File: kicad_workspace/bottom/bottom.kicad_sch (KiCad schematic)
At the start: 11 parts, among them M1 N20_MOTOR_EXTENDED_SHAFT, M2 N20_MOTOR_EXTENDED_SHAFT, U1 DRV8833PWP, U2 ULTRASOUND_T_R, U3 ATmega4809-A

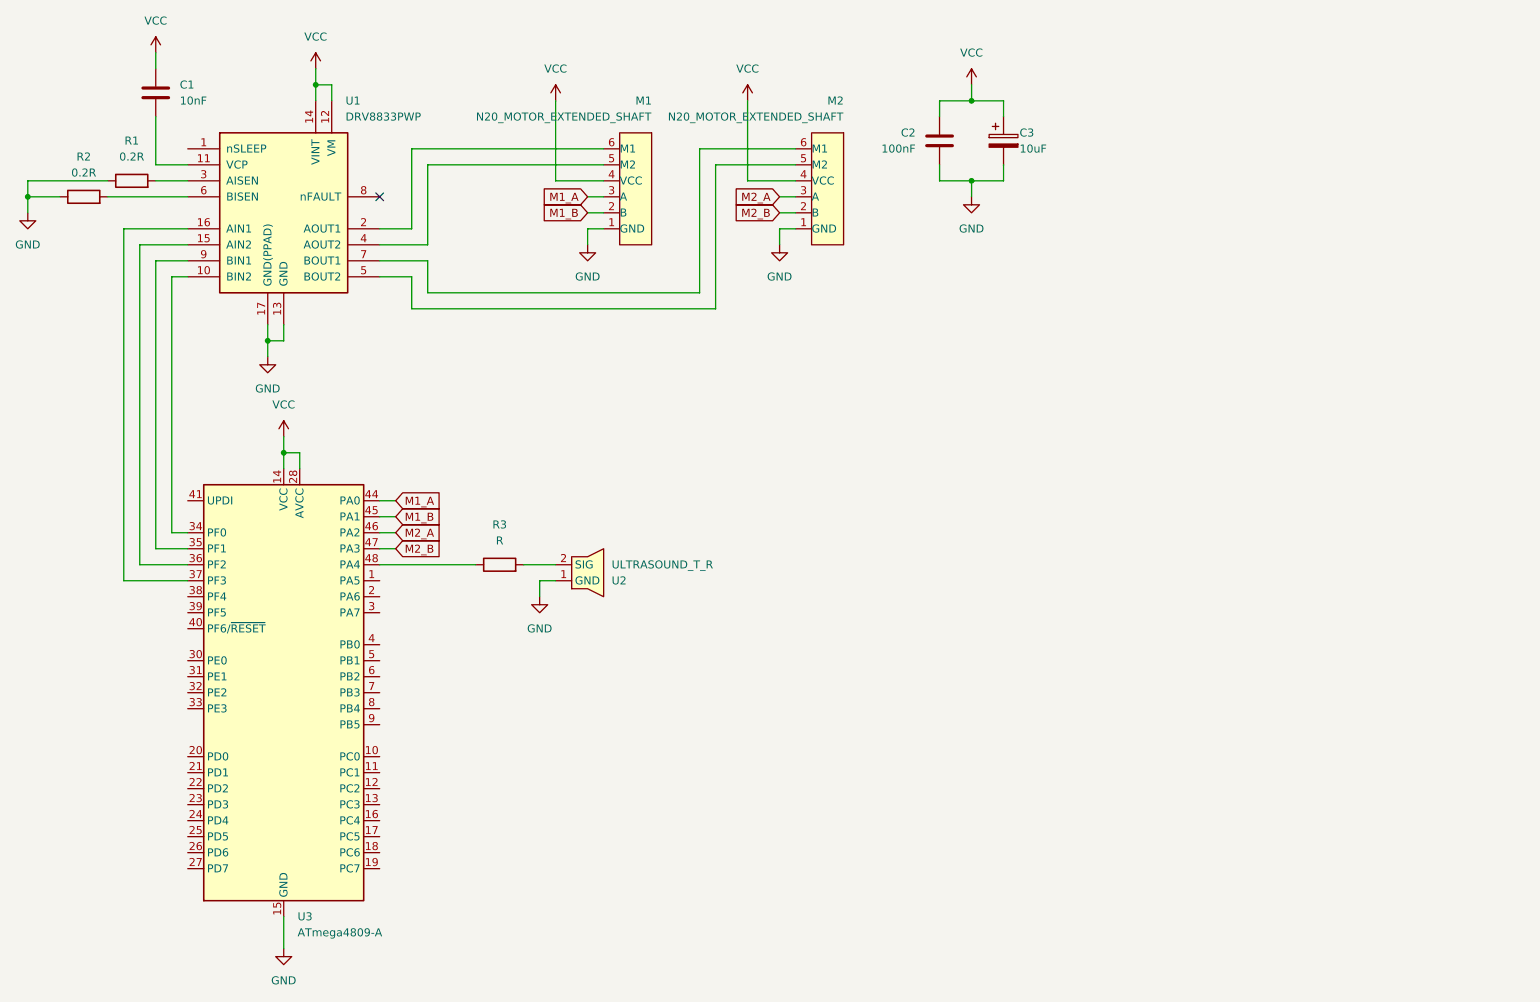
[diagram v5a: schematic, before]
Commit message: add bno055 - acc ic
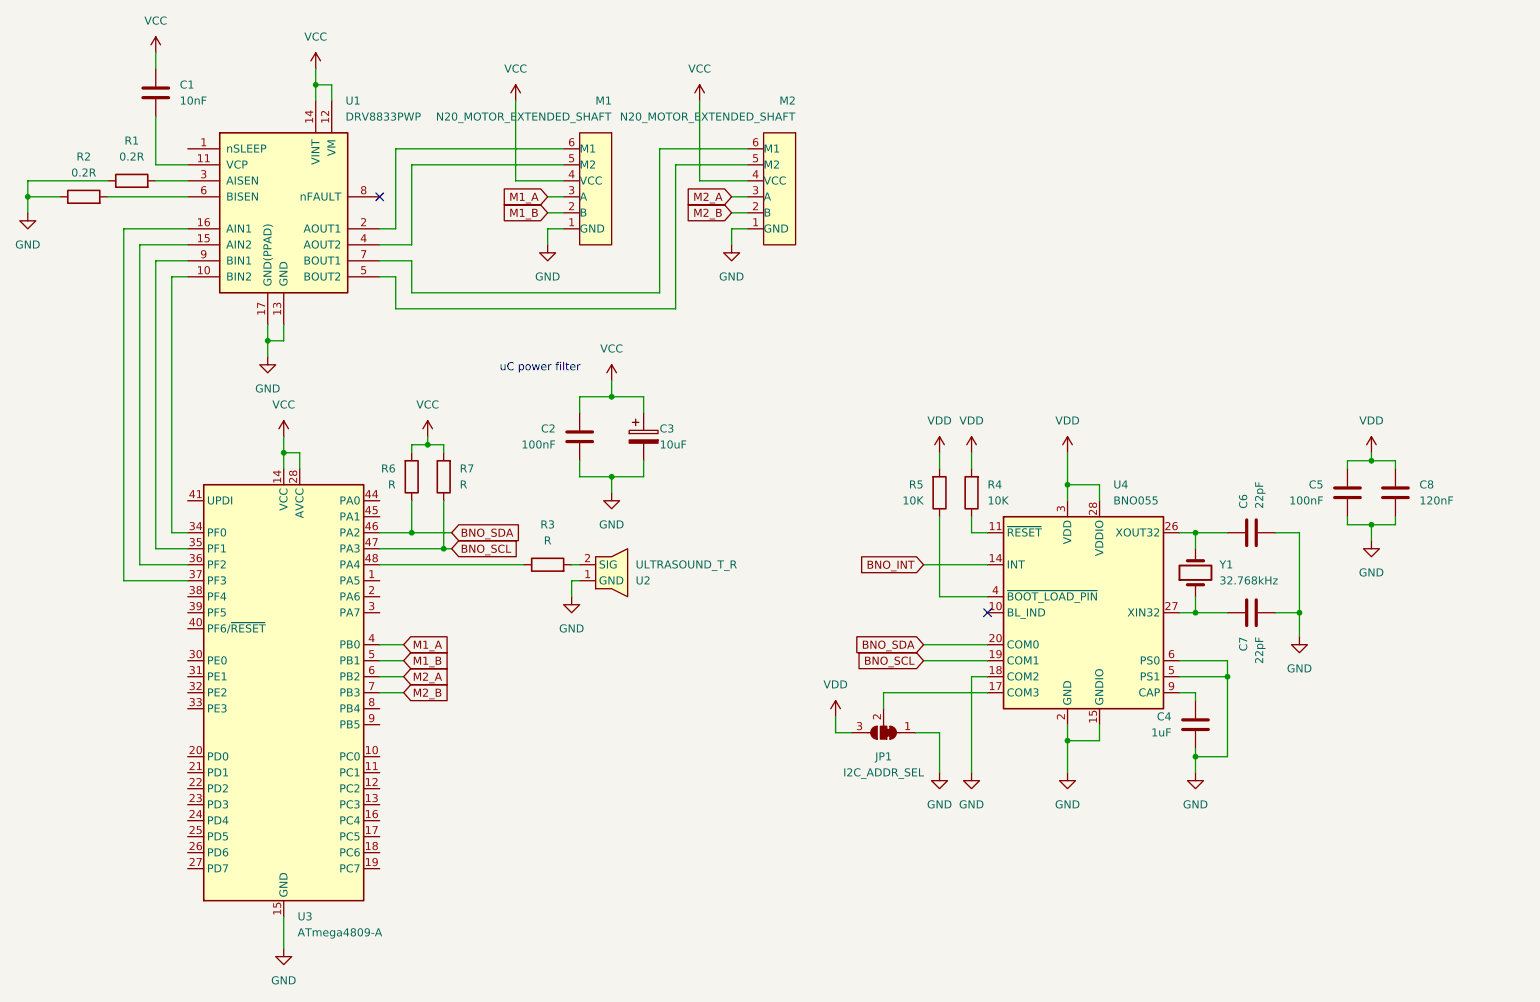
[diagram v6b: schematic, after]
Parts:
- added C4: 1uF, symbol Device:C
- added C5: 100nF, symbol Device:C
- added C6, C7: 22pF, symbol Device:C
- added C8: 120nF, symbol Device:C
- added JP1: I2C_ADDR_SEL, Jumper:SolderJumper-3_P1.3mm_Bridged12_Pad1.0x1.5mm_NumberLabels, symbol Jumper:SolderJumper_3_Bridged12
- added R4, R5: 10K, symbol Device:R
- added R6, R7: R, symbol Device:R
- added U4: BNO055, Package_LGA:LGA-28_5.2x3.8mm_P0.5mm, symbol Sensor_Motion:BNO055
- added Y1: 32.768kHz, Crystal:Crystal_SMD_MicroCrystal_CM9V-T1A-2Pin_1.6x1.0mm, symbol Device:Crystal
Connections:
- net GND: now also C4.2, C5.2, C6.2, C7.2, C8.2, JP1.1 (A), U4.15 (GNDIO), U4.16 (GNDIO), U4.18 (COM2), U4.2 (GND), U4.25 (GNDIO), U4.5 (PS1), U4.6 (PS0)
- net M1_A: now also U3.4 (PB0); no longer U3.44 (PA0)
- net M1_B: now also U3.5 (PB1); no longer U3.45 (PA1)
- net M2_A: now also U3.6 (PB2); no longer U3.46 (PA2)
- net M2_B: now also U3.7 (PB3); no longer U3.47 (PA3)
- net VCC: now also R6.2, R7.2
- new net: C7.1, U4.27 (XIN32), Y1.1
- new net: R4.1, U4.11 (~{RESET})
- new net: C4.1, U4.9 (CAP)
- new net: C6.1, U4.26 (XOUT32), Y1.2
- new net: R5.1, U4.4 (~{BOOT_LOAD_PIN})
- new net: JP1.2 (C), U4.17 (COM3)
- new net BNO_INT: U4.14 (INT)
- new net BNO_SCL: R7.1, U3.47 (PA3), U4.19 (COM1)
- new net BNO_SDA: R6.1, U3.46 (PA2), U4.20 (COM0)
- new net VDD: C5.1, C8.1, JP1.3 (B), R4.2, R5.2, U4.28 (VDDIO), U4.3 (VDD)
- no-connect marks 1 -> 2
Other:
- note added: "uC power filter"
- moved on the sheet: C2, C3, M1, M2, R3, U2

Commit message: small schematic fixes (NC)
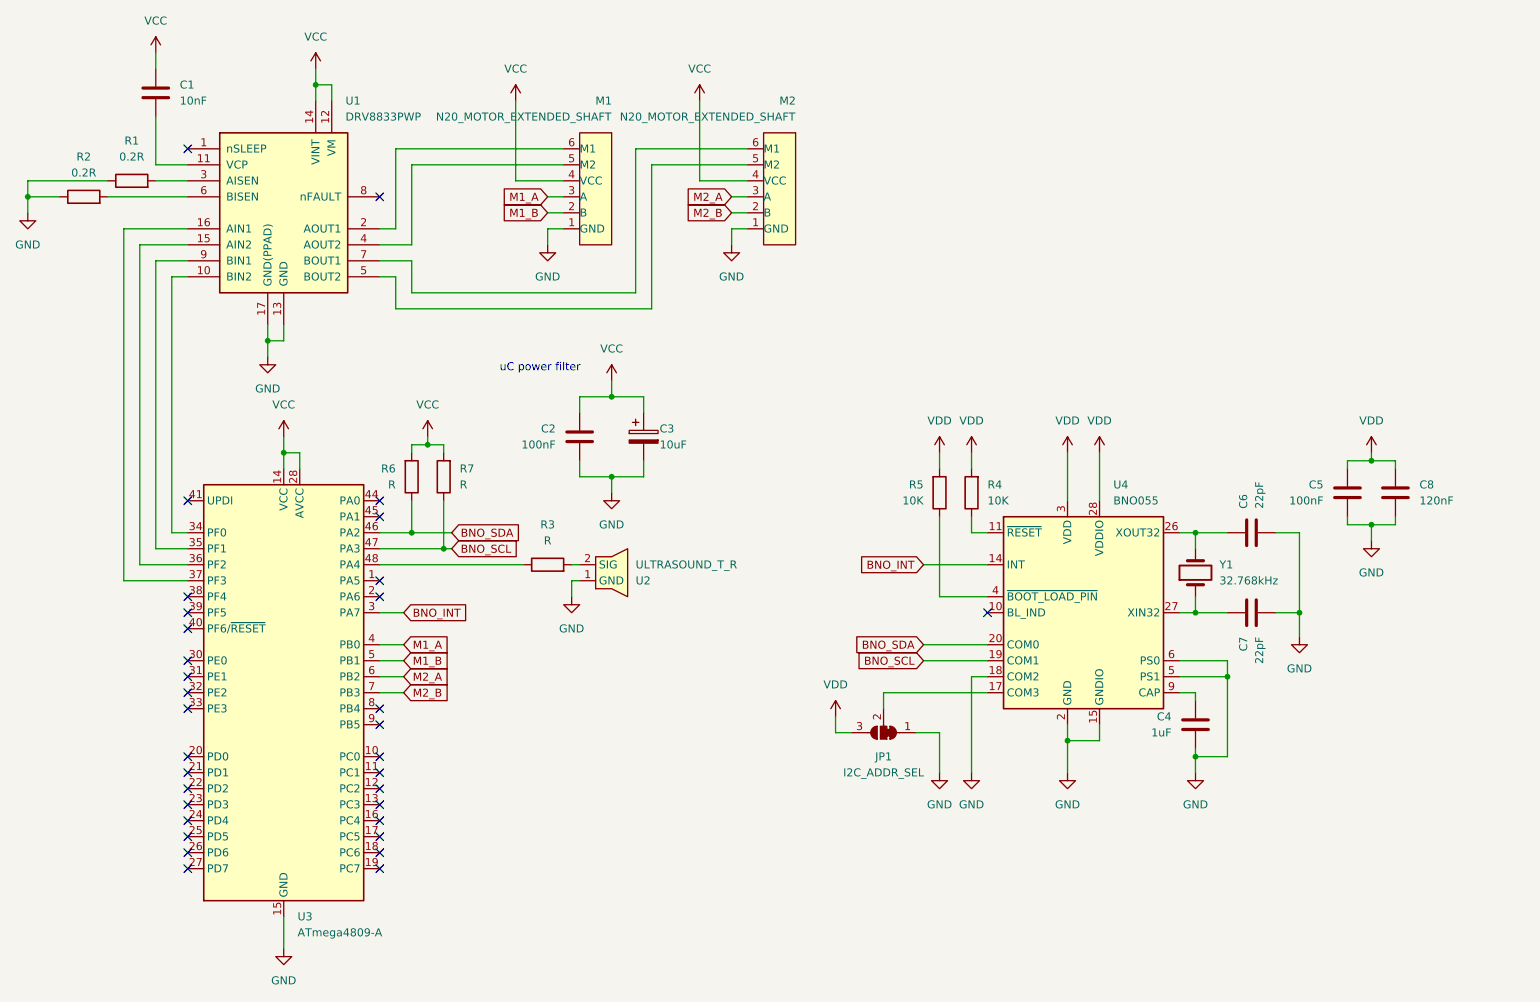
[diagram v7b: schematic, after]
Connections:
- net BNO_INT: now also U3.3 (PA7)
- no-connect marks 2 -> 33
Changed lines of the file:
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@@
   (junction (at 227.33 114.3) (diameter 0) (color 0 0 0 0)
   )
-  (junction (at 190.5 93.98) (diameter 0) (color 0 0 0 0)
-  )
+  (no_connect (at 81.28 129.54))
+  (no_connect (at 50.8 116.84))
+  (no_connect (at 50.8 124.46))
+  (no_connect (at 81.28 137.16))
   (no_connect (at 81.28 48.26))
+  (no_connect (at 50.8 114.3))
+  (no_connect (at 50.8 142.24))
+  (no_connect (at 50.8 152.4))
+  (no_connect (at 50.8 139.7))
   (no_connect (at 177.8 114.3))
+  (no_connect (at 50.8 149.86))
+  (no_connect (at 81.28 144.78))
+  (no_connect (at 50.8 127))
+  (no_connect (at 81.28 132.08))
+  (no_connect (at 50.8 147.32))
+  (no_connect (at 50.8 96.52))
+  (no_connect (at 50.8 137.16))
+  (no_connect (at 81.28 149.86))
+  (no_connect (at 81.28 109.22))
+  (no_connect (at 50.8 111.76))
+  (no_connect (at 50.8 121.92))
+  (no_connect (at 81.28 154.94))
+  (no_connect (at 81.28 111.76))
+  (no_connect (at 81.28 142.24))
+  (no_connect (at 50.8 40.64))
+  (no_connect (at 81.28 139.7))
+  (no_connect (at 50.8 154.94))
+  (no_connect (at 50.8 144.78))
+  (no_connect (at 81.28 96.52))
+  (no_connect (at 81.28 147.32))
+  (no_connect (at 81.28 99.06))
+  (no_connect (at 50.8 129.54))
+  (no_connect (at 81.28 152.4))
+  (wire (pts (xy 81.28 60.96) (xy 83.82 60.96))
+    (stroke (width 0) (type default))
+  )
   (wire (pts (xy 66.04 68.58) (xy 66.04 71.12))
     (stroke (width 0) (type default))
@@
     (stroke (width 0) (type default))
   )
+  (wire (pts (xy 81.28 114.3) (xy 85.09 114.3))
+    (stroke (width 0) (type default))
+  )
   (wire (pts (xy 123.19 90.17) (xy 123.19 92.71))
     (stroke (width 0) (type default))
@@
     (stroke (width 0) (type default))
   )
+  (wire (pts (xy 121.92 63.5) (xy 121.92 40.64))
+    (stroke (width 0) (type default))
+  )
   (wire (pts (xy 111.76 109.22) (xy 113.03 109.22))
     (stroke (width 0) (type default))
@@
     (stroke (width 0) (type default))
   )
-  (wire (pts (xy 195.58 96.52) (xy 195.58 93.98))
-    (stroke (width 0) (type default))
-  )
   (wire (pts (xy 161.29 127) (xy 161.29 129.54))
     (stroke (width 0) (type default))
   )
-  (wire (pts (xy 128.27 66.04) (xy 128.27 43.18))
+  (wire (pts (xy 195.58 88.9) (xy 195.58 96.52))
     (stroke (width 0) (type default))
   )
@@
     (stroke (width 0) (type default))
   )
+  (wire (pts (xy 124.46 43.18) (xy 139.7 43.18))
+    (stroke (width 0) (type default))
+  )
   (wire (pts (xy 25.4 48.26) (xy 25.4 50.8))
     (stroke (width 0) (type default))
   )
-  (wire (pts (xy 86.36 63.5) (xy 125.73 63.5))
-    (stroke (width 0) (type default))
-  )
   (wire (pts (xy 175.26 88.9) (xy 175.26 91.44))
     (stroke (width 0) (type default))
@@
     (stroke (width 0) (type default))
   )
-  (wire (pts (xy 128.27 43.18) (xy 139.7 43.18))
-    (stroke (width 0) (type default))
-  )
   (wire (pts (xy 63.5 71.12) (xy 66.04 71.12))
     (stroke (width 0) (type default))
@@
     (stroke (width 0) (type default))
   )
+  (wire (pts (xy 83.82 60.96) (xy 83.82 66.04))
+    (stroke (width 0) (type default))
+  )
   (wire (pts (xy 50.8 55.88) (xy 43.18 55.88))
     (stroke (width 0) (type default))
   )
-  (wire (pts (xy 190.5 93.98) (xy 190.5 96.52))
-    (stroke (width 0) (type default))
-  )
-  (wire (pts (xy 190.5 88.9) (xy 190.5 93.98))
+  (wire (pts (xy 190.5 88.9) (xy 190.5 96.52))
     (stroke (width 0) (type default))
   )
@@
     (stroke (width 0) (type default))
   )
-  (wire (pts (xy 83.82 60.96) (xy 83.82 66.04))
-    (stroke (width 0) (type default))
-  )
   (wire (pts (xy 63.5 71.12) (xy 63.5 73.66))
     (stroke (width 0) (type default))
@@
     (stroke (width 0) (type default))
   )
+  (wire (pts (xy 83.82 66.04) (xy 124.46 66.04))
+    (stroke (width 0) (type default))
+  )
   (wire (pts (xy 113.03 90.17) (xy 113.03 92.71))
     (stroke (width 0) (type default))
@@
     (stroke (width 0) (type default))
   )
+  (wire (pts (xy 215.9 137.16) (xy 210.82 137.16))
+    (stroke (width 0) (type default))
+  )
+  (wire (pts (xy 45.72 43.18) (xy 50.8 43.18))
+    (stroke (width 0) (type default))
+  )
+  (wire (pts (xy 170.18 88.9) (xy 170.18 91.44))
+    (stroke (width 0) (type default))
+  )
+  (wire (pts (xy 40.64 53.34) (xy 40.64 109.22))
+    (stroke (width 0) (type default))
+  )
+  (wire (pts (xy 25.4 45.72) (xy 25.4 48.26))
+    (stroke (width 0) (type default))
+  )
+  (wire (pts (xy 81.28 119.38) (xy 85.09 119.38))
+    (stroke (width 0) (type default))
+  )
   (wire (pts (xy 86.36 58.42) (xy 86.36 63.5))
     (stroke (width 0) (type default))
   )
-  (wire (pts (xy 215.9 137.16) (xy 210.82 137.16))
-    (stroke (width 0) (type default))
-  )
-  (wire (pts (xy 45.72 43.18) (xy 50.8 43.18))
-    (stroke (width 0) (type default))
-  )
-  (wire (pts (xy 170.18 88.9) (xy 170.18 91.44))
-    (stroke (width 0) (type default))
-  )
-  (wire (pts (xy 40.64 53.34) (xy 40.64 109.22))
-    (stroke (width 0) (type default))
-  )
-  (wire (pts (xy 25.4 45.72) (xy 25.4 48.26))
-    (stroke (width 0) (type default))
-  )
-  (wire (pts (xy 81.28 119.38) (xy 85.09 119.38))
-    (stroke (width 0) (type default))
-  )
   (wire (pts (xy 107.95 48.26) (xy 110.49 48.26))
     (stroke (width 0) (type default))
@@
     (stroke (width 0) (type default))
   )
-  (wire (pts (xy 83.82 60.96) (xy 81.28 60.96))
-    (stroke (width 0) (type default))
-  )
   (wire (pts (xy 210.82 101.6) (xy 215.9 101.6))
     (stroke (width 0) (type default))
@@
     (stroke (width 0) (type default))
   )
-  (wire (pts (xy 83.82 66.04) (xy 128.27 66.04))
-    (stroke (width 0) (type default))
-  )
   (wire (pts (xy 153.67 133.35) (xy 156.21 133.35))
     (stroke (width 0) (type default))
@@
     (stroke (width 0) (type default))
   )
-  (wire (pts (xy 125.73 63.5) (xy 125.73 40.64))
+  (wire (pts (xy 81.28 58.42) (xy 86.36 58.42))
     (stroke (width 0) (type default))
   )
@@
     (stroke (width 0) (type default))
   )
-  (wire (pts (xy 195.58 93.98) (xy 190.5 93.98))
+  (wire (pts (xy 86.36 63.5) (xy 121.92 63.5))
     (stroke (width 0) (type default))
   )
@@
     (stroke (width 0) (type default))
   )
-  (wire (pts (xy 81.28 58.42) (xy 86.36 58.42))
-    (stroke (width 0) (type default))
-  )
   (wire (pts (xy 45.72 45.72) (xy 50.8 45.72))
     (stroke (width 0) (type default))
@@
     (stroke (width 0) (type default))
   )
+  (wire (pts (xy 121.92 40.64) (xy 139.7 40.64))
+    (stroke (width 0) (type default))
+  )
   (wire (pts (xy 83.82 53.34) (xy 81.28 53.34))
     (stroke (width 0) (type default))
@@
     (stroke (width 0) (type default))
   )
+  (wire (pts (xy 124.46 66.04) (xy 124.46 43.18))
+    (stroke (width 0) (type default))
+  )
   (wire (pts (xy 210.82 114.3) (xy 210.82 111.76))
-    (stroke (width 0) (type default))
-  )
-  (wire (pts (xy 125.73 40.64) (xy 139.7 40.64))
     (stroke (width 0) (type default))
   )
@@
     (effects (font (size 1.27 1.27)) (justify left))
     (property "Intersheetrefs" "${INTERSHEET_REFS}" (at 92.7923 119.38 0)
+      (effects (font (size 1.27 1.27)) (justify left) hide)
+    )
+  )
+  (global_label "BNO_INT" (shape input) (at 85.09 114.3 0) (fields_autoplaced)
+    (effects (font (size 1.27 1.27)) (justify left))
+    (property "Intersheetrefs" "${INTERSHEET_REFS}" (at 95.8767 114.3 0)
       (effects (font (size 1.27 1.27)) (justify left) hide)
     )
@@
         )
       )
+    )
+  )
+  (symbol (lib_id "power:VDD") (at 195.58 88.9 0) (unit 1)
+    (in_bom yes) (on_board yes) (dnp no) (fields_autoplaced)
+    (property "Reference" "#PWR024" (at 195.58 92.71 0)
+      (effects (font (size 1.27 1.27)) hide)
+    )
+    (property "Value" "VDD" (at 195.58 83.82 0)
+      (effects (font (size 1.27 1.27)))
+    )
+    (property "Footprint" "" (at 195.58 88.9 0)
+      (effects (font (size 1.27 1.27)) hide)
+    )
+    (property "Datasheet" "" (at 195.58 88.9 0)
+      (effects (font (size 1.27 1.27)) hide)
+    )
+    (pin "1")
+    (instances
+      (project "bottom"
+        (path "/8949e4cc-98fb-401d-bf78-7a26c685fd98"
+          (reference "#PWR024") (unit 1)
+        )
+      )

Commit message: add vl53l0x to schematic, connect footprint to sensors symbol
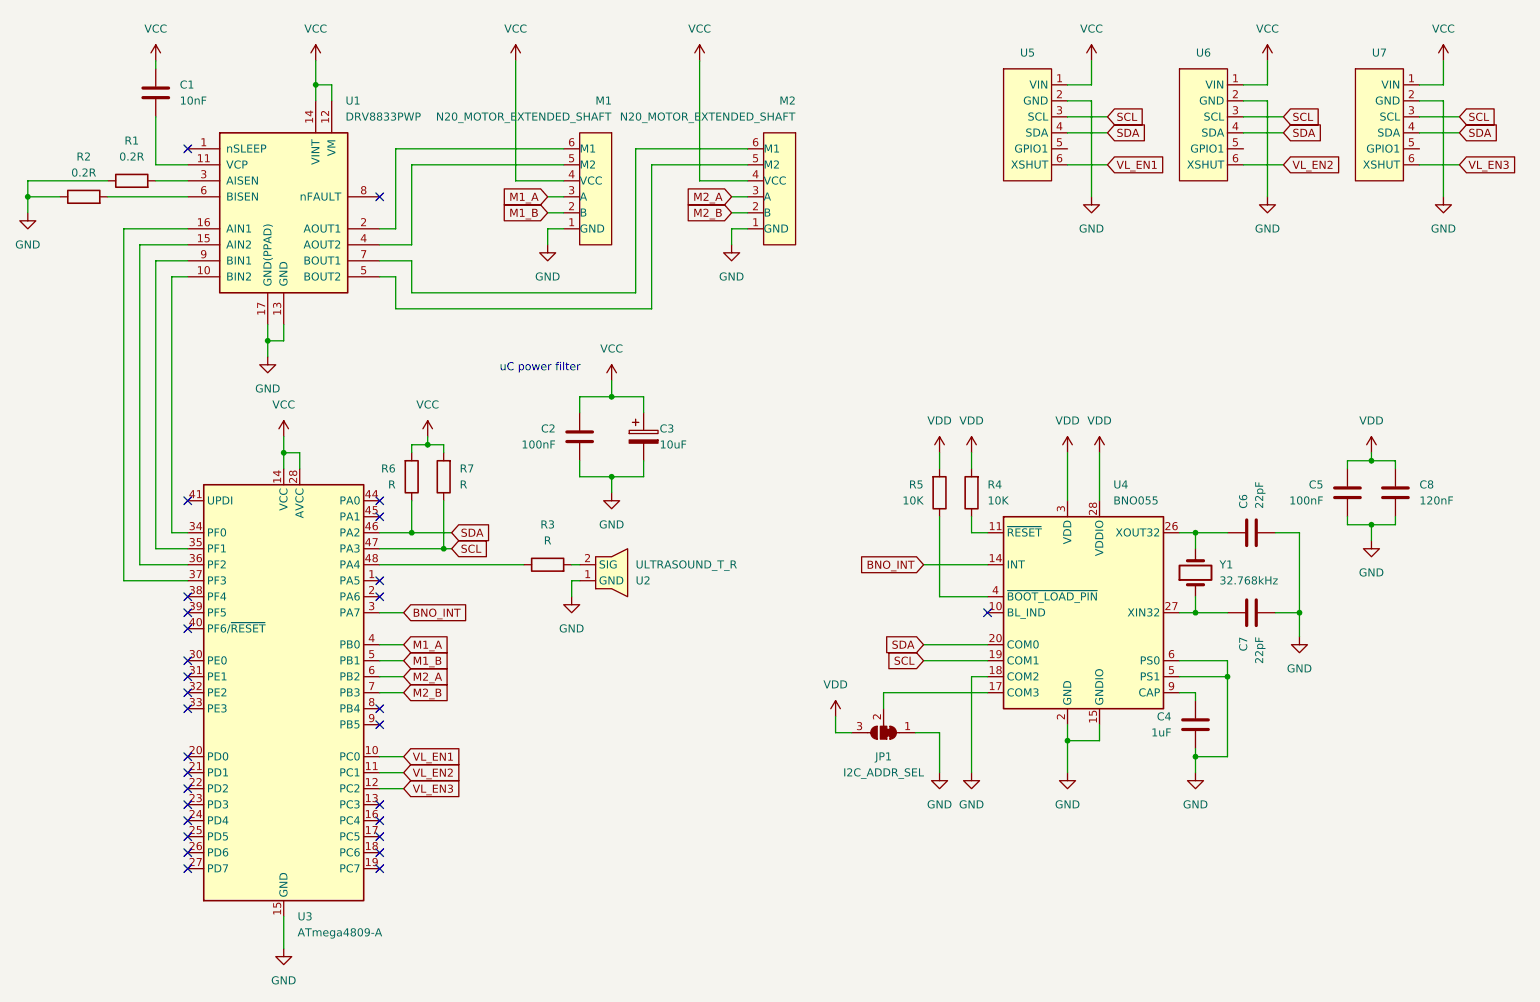
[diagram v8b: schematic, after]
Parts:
- added U5, U6, U7: ~, pololu:VL53L0X, symbol pololu:VL53L0X
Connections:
- net GND: now also U5.2 (GND), U6.2 (GND), U7.2 (GND)
- net VCC: now also U5.1 (VIN), U6.1 (VIN), U7.1 (VIN)
- net VL_EN1: now reaches U3.10 (PC0)
- net VL_EN1: now also U5.6 (XSHUT)
- net VL_EN2: now reaches U3.11 (PC1)
- net VL_EN2: now also U6.6 (XSHUT)
- net VL_EN3: now reaches U3.12 (PC2)
- net VL_EN3: now also U7.6 (XSHUT)
- net BNO_SCL renamed SCL
- net SCL: now also U5.3 (SCL), U6.3 (SCL), U7.3 (SCL)
- net BNO_SDA renamed SDA
- net SDA: now also U5.4 (SDA), U6.4 (SDA), U7.4 (SDA)
- no-connect marks 33 -> 30
